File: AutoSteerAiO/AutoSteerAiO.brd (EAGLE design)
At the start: 114.3 x 99.1 mm, 88 parts, among them J4 CONNECTOR 1x5 PINS, K4 CB1A-P-12V, T1 BC547, U1 VX7805-1000

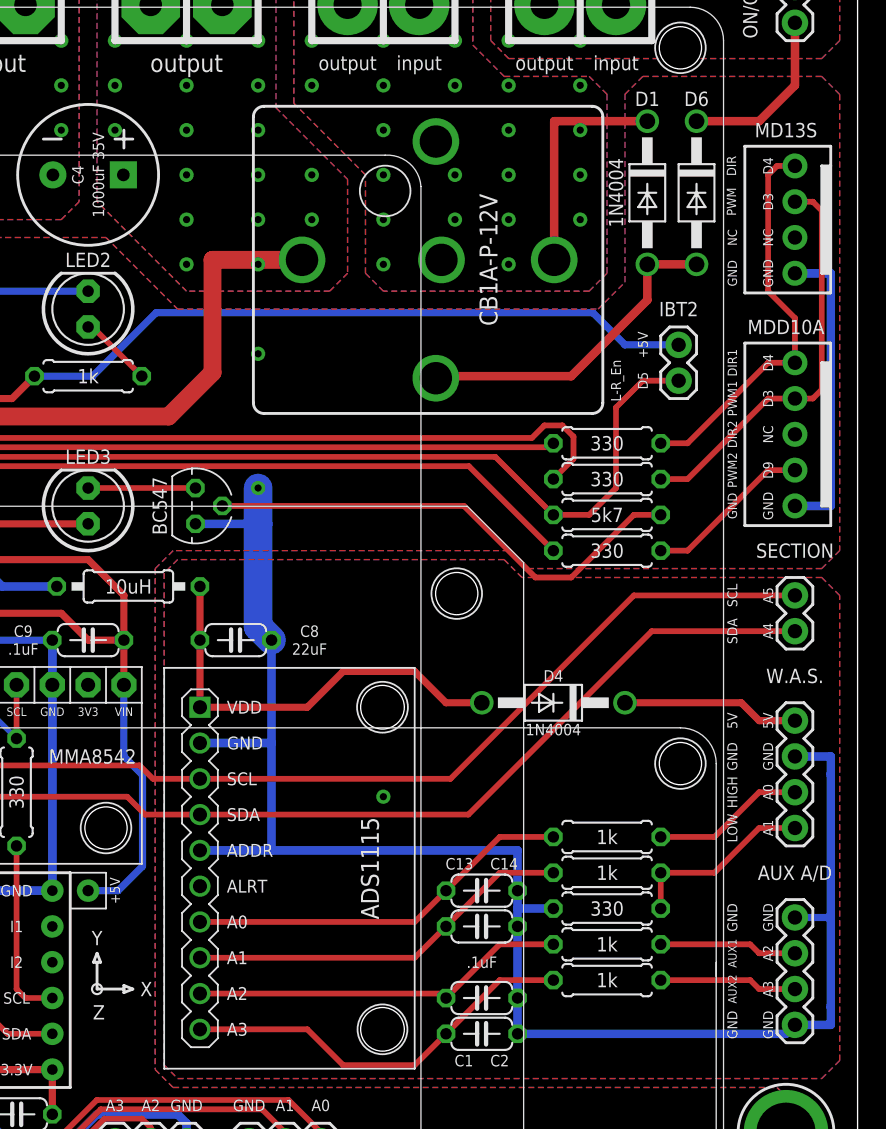
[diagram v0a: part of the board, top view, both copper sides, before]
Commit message: Add files via upload
One connector for all motor drivers
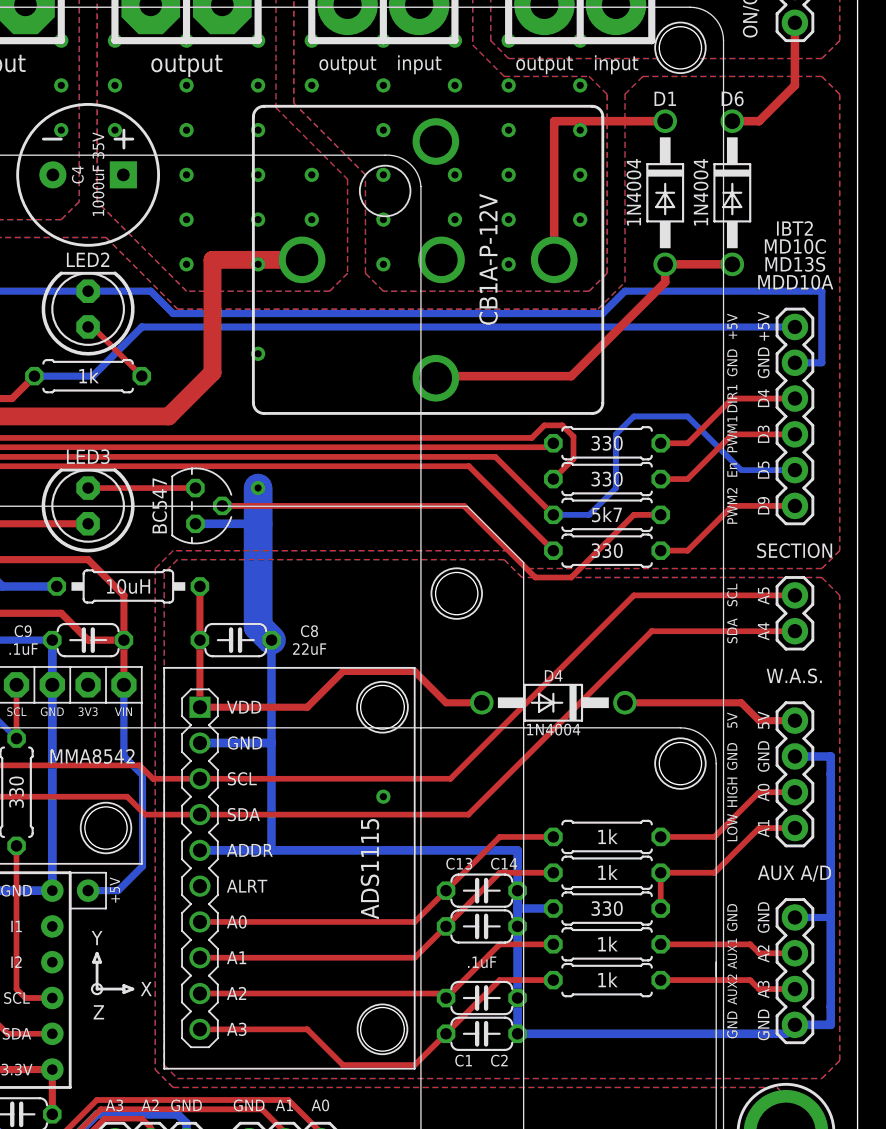
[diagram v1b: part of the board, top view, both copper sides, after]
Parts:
- removed D5: CONNECTOR 1x1 PIN, SparkFun-Connectors:1X02
- removed JP1: CONNECTOR 1x4 PINS, Header and Connector:2600-04
- J4: device Header and Connector:2600-05 -> SparkFun-Connectors:1X06
- moved D6 2.54 mm to (105.4, 71.8)
- moved D1 1.27 mm to (100.6, 71.8)
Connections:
- net +5V: now also J4.6; no longer D5.2
- net D5: now also J4.2; no longer D5.1
- net GND: now also J4.5; no longer J4.1, JP1.1
- net N$19: now also J4.4; no longer J4.5, JP1.4
- net N$20: now also J4.3; no longer J4.4, JP1.3
- net N$22: now also J4.1; no longer J4.2
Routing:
- net GND: track 526.2 -> 565.0 mm
- net N$20: track 28.9 -> 10.8 mm
- net N$19: track 28.2 -> 10.8 mm
- net D5: track 103.6 -> 111.2 mm
- net +5V: track 316.5 -> 323.4 mm
- net N$28: track 12.5 -> 9.94 mm
- net N$5: track 23.4 -> 25.2 mm
- net V+: track 16.4 -> 17.7 mm
- net N$22: track 11.9 -> 10.8 mm
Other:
- board text added: "D5"
- board text added: "En"
- board text removed: "DIR"
- board text removed: "DIR2"
- board text removed: "L-R_En"
- board text removed: "NC"
- board text removed: "PWM"

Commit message: Add files via upload
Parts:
- removed 15V1, 15V2, GND, GND30: WIREPAD4,16O1,6, wirepad:4,16O1,6
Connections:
- net +15V: no longer 15V1.1, 15V2.1
- net GND: no longer GND.1, GND30.1
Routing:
- net GND: vias 70 -> 72
- net +15V: vias 20 -> 22
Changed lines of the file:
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@@
 <setting verticaltext="up"/>
 </settings>
-<grid distance="50" unitdist="mil" unit="mil" style="lines" multiple="1" display="yes" altdistance="12.5" altunitdist="mil" altunit="mil"/>
+<grid distance="50" unitdist="mil" unit="mm" style="lines" multiple="1" display="yes" altdistance="12.5" altunitdist="mil" altunit="mil"/>
 <layers>
 <layer number="1" name="Top" color="4" fill="1" visible="yes" active="yes"/>
@@
 <attribute name="OC_NEWARK" value="unknown" x="109.855" y="86.36" size="1.778" layer="27" rot="R270" display="off"/>
 </element>
-<element name="15V1" library="wirepad" library_urn="urn:adsk.eagle:library:412" package="4,16O1,6" package3d_urn="urn:adsk.eagle:package:30843/1" value="WIREPAD4,16O1,6" x="69.215" y="85.09" smashed="yes" rot="R180">
-<attribute name="MF" value="" x="69.215" y="85.09" size="1.778" layer="27" rot="R180" display="off"/>
-<attribute name="MPN" value="" x="69.215" y="85.09" size="1.778" layer="27" rot="R180" display="off"/>
-<attribute name="OC_NEWARK" value="unknown" x="69.215" y="85.09" size="1.778" layer="27" rot="R180" display="off"/>
-</element>
-<element name="15V2" library="wirepad" library_urn="urn:adsk.eagle:library:412" package="4,16O1,6" package3d_urn="urn:adsk.eagle:package:30843/1" value="WIREPAD4,16O1,6" x="64.135" y="85.09" smashed="yes" rot="R180">
-<attribute name="MF" value="" x="64.135" y="85.09" size="1.778" layer="27" rot="R180" display="off"/>
-<attribute name="MPN" value="" x="64.135" y="85.09" size="1.778" layer="27" rot="R180" display="off"/>
-<attribute name="OC_NEWARK" value="unknown" x="64.135" y="85.09" size="1.778" layer="27" rot="R180" display="off"/>
-</element>
-<element name="GND" library="wirepad" library_urn="urn:adsk.eagle:library:412" package="4,16O1,6" package3d_urn="urn:adsk.eagle:package:30843/1" value="WIREPAD4,16O1,6" x="55.245" y="85.09" smashed="yes" rot="R180">
-<attribute name="MF" value="" x="55.245" y="85.09" size="1.778" layer="27" rot="R180" display="off"/>
-<attribute name="MPN" value="" x="55.245" y="85.09" size="1.778" layer="27" rot="R180" display="off"/>
-<attribute name="OC_NEWARK" value="unknown" x="55.245" y="85.09" size="1.778" layer="27" rot="R180" display="off"/>
-</element>
-<element name="GND30" library="wirepad" library_urn="urn:adsk.eagle:library:412" package="4,16O1,6" package3d_urn="urn:adsk.eagle:package:30843/1" value="WIREPAD4,16O1,6" x="50.165" y="85.09" smashed="yes" rot="R180">
-<attribute name="MF" value="" x="50.165" y="85.09" size="1.778" layer="27" rot="R180" display="off"/>
-<attribute name="MPN" value="" x="50.165" y="85.09" size="1.778" layer="27" rot="R180" display="off"/>
-<attribute name="OC_NEWARK" value="unknown" x="50.165" y="85.09" size="1.778" layer="27" rot="R180" display="off"/>
-</element>
 <element name="J4" library="SparkFun-Connectors" library_urn="urn:adsk.eagle:library:513" package="1X06" package3d_urn="urn:adsk.eagle:package:38009/1" value="CONNECTOR 1x5 PINS" x="109.855" y="49.53" smashed="yes" rot="R90">
 <attribute name="LABEL" value="" x="112.776" y="48.133" size="0.762" layer="21" font="vector" ratio="15" rot="R90" align="top-left"/>
@@
 <contactref element="C12" pad="1"/>
 <contactref element="C4" pad="-"/>
-<contactref element="GND30" pad="1"/>
-<contactref element="GND" pad="1"/>
 <contactref element="D3" pad="A"/>
 <contactref element="LED1" pad="K"/>
@@
 <via x="8.89" y="2.54" extent="1-16" drill="0.508"/>
 <via x="26.67" y="29.845" extent="1-16" drill="0.508"/>
-<via x="92.075" y="85.09" extent="1-16" drill="2" diameter="4.3" shape="square"/>
-<via x="97.155" y="85.09" extent="1-16" drill="2" diameter="4.3" shape="square"/>
+<via x="92.075" y="85.09" extent="1-16" drill="2.8" diameter="4.5" shape="square"/>
+<via x="97.155" y="85.09" extent="1-16" drill="2.8" diameter="4.5" shape="square"/>
 <contactref element="C5" pad="-"/>
 <via x="89.535" y="82.55" extent="1-16" drill="0.508"/>
@@
 <wire x1="111.76" y1="59.69" x2="111.76" y2="64.77" width="0.508" layer="16"/>
 <wire x1="111.76" y1="64.77" x2="97.79" y2="64.77" width="0.508" layer="16"/>
+<via x="55.245" y="85.09" extent="1-16" drill="2.8" diameter="4.5" shape="square"/>
+<via x="50.165" y="85.09" extent="1-16" drill="2.8" diameter="4.5" shape="square"/>
 </signal>
 <signal name="D5">
@@
 </signal>
 <signal name="V+">
-<via x="83.185" y="85.09" extent="1-16" drill="2" diameter="4.3" shape="square"/>
-<via x="78.105" y="85.09" extent="1-16" drill="2" diameter="4.3" shape="square" alwaysstop="yes"/>
+<via x="83.185" y="85.09" extent="1-16" drill="2.8" diameter="4.5" shape="square"/>
+<via x="78.105" y="85.09" extent="1-16" drill="2.8" diameter="4.5" shape="square" alwaysstop="yes"/>
 <contactref element="K4" pad="87"/>
 <contactref element="K4" pad="85"/>
@@
 <signal name="+15V">
 <contactref element="C4" pad="+"/>
-<contactref element="15V1" pad="1"/>
-<contactref element="15V2" pad="1"/>
 <contactref element="R12" pad="1"/>
 <contactref element="R13" pad="1"/>
@@
 <wire x1="10.16" y1="18.415" x2="6.35" y2="18.415" width="0.6096" layer="1"/>
 <wire x1="6.35" y1="18.415" x2="5.08" y2="17.145" width="0.6096" layer="1"/>
+<via x="69.215" y="85.09" extent="1-16" drill="2.8" diameter="4.5" shape="square"/>
+<via x="64.135" y="85.09" extent="1-16" drill="2.8" diameter="4.5" shape="square"/>
 </signal>
 <signal name="HIGH">

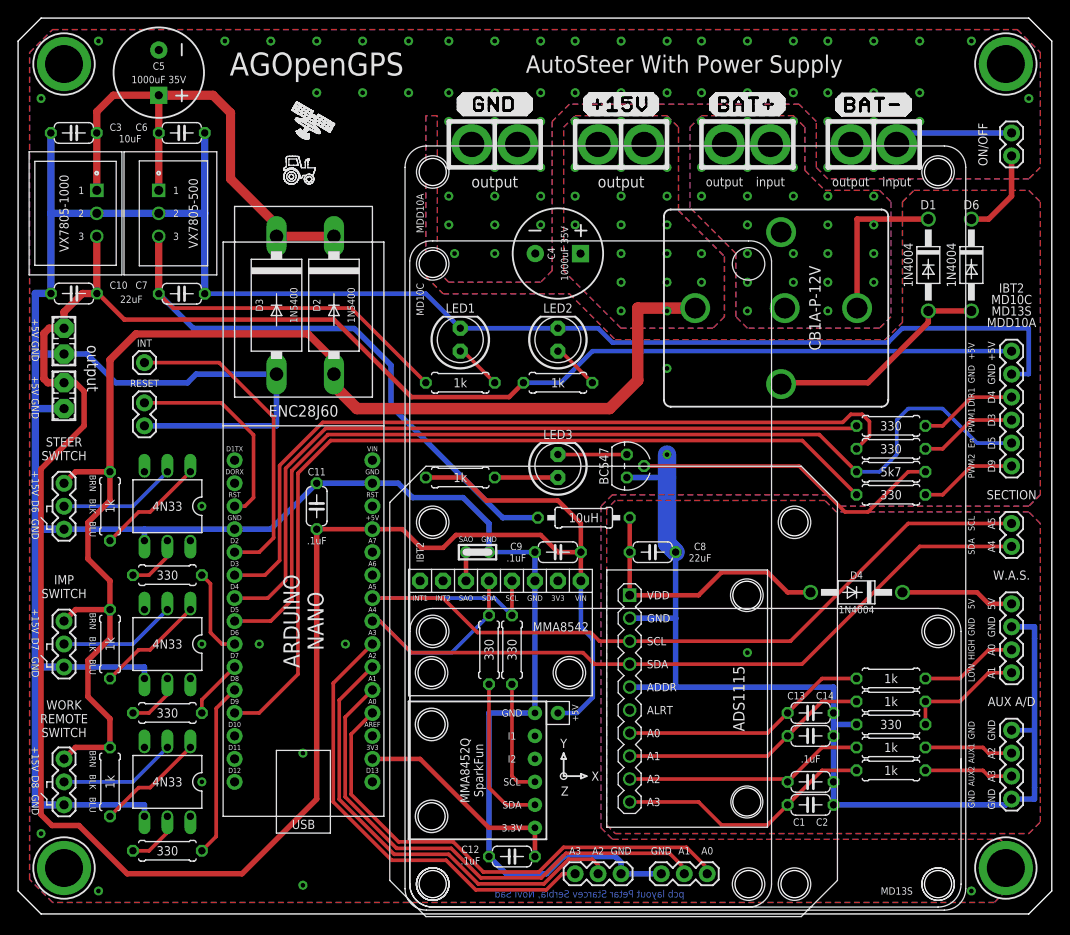
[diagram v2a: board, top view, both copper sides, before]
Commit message: Add files via upload
Added connector for SWEncoder
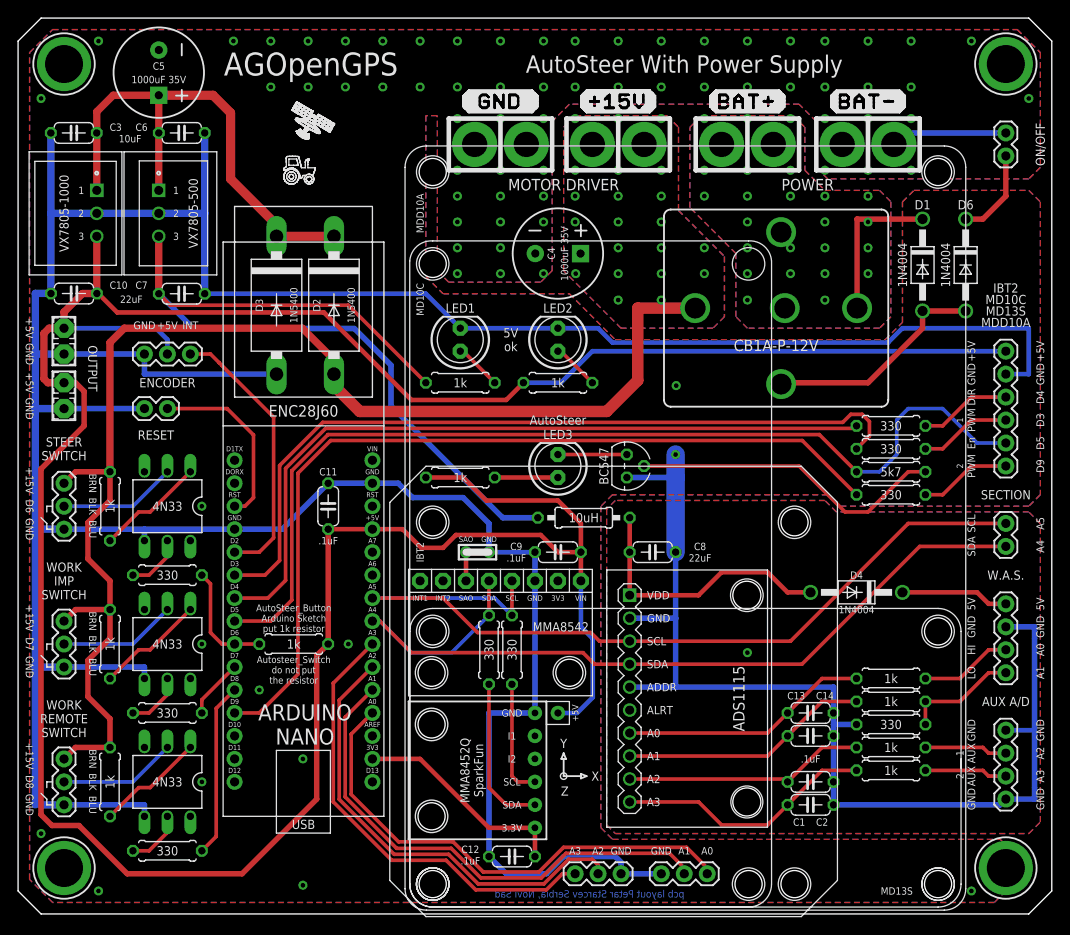
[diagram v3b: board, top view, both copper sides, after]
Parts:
- added R15: 1k, resistor:0207/7
- INT: value CONNECTOR 1x1 PIN -> (none); device SparkFun-Connectors:1X01 -> SparkFun-Connectors:1X03
- moved INT 5.17 mm to (19.1, 61.9), turned to 180 degrees
- moved RESET 1.91 mm to (14.0, 55.9), turned to 0 degrees
- moved U$11 1.91 mm to (78.1, 54.0)
- moved C11 1.27 mm to (34.3, 45.1)
- moved U$12 1.27 mm to (80.6, 48.9)
- moved AUX_A/D 0.64 mm to (109.2, 12.7)
- moved J4 0.64 mm to (109.2, 49.5)
- moved ON/OFF 0.64 mm to (109.2, 86.4)
- moved TO_SECTION 0.64 mm to (109.2, 43.2)
- moved WAS_D 0.64 mm to (109.2, 34.3)
- moved D1 0.63 mm to (100.0, 71.8)
- moved D6 0.63 mm to (104.8, 71.8)
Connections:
- net +5V: now also INT.2, R15.1
- net D6: now also R15.2
- net GND: now also INT.3
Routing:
- net +5V: track 323.4 -> 335.8 mm
- net GND: track 565.0 -> 556.2 mm, vias 72 -> 80
- net D2: track 35.1 -> 30.4 mm
- net RST: track 22.9 -> 20.1 mm
- net D6: track 9.94 -> 12.7 mm
- net +15V: track 144.0 -> 145.9 mm, vias 22 -> 23
- net SCL: track 98.1 -> 97.4 mm
- net SDA: track 97.9 -> 97.3 mm
- net N$22: track 10.8 -> 10.2 mm
- net N$21: track 12.6 -> 12.0 mm
- net N$20: track 10.8 -> 10.2 mm
- net N$19: track 10.8 -> 10.2 mm
- net N$11: track 9.79 -> 9.15 mm
- net N$10: track 9.79 -> 9.15 mm
- net LOW.: track 13.4 -> 12.7 mm
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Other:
- board text added: "1"
- board text added: "1k"
- board text added: "2"
- board text added: "5V ok"
- board text added: "AUX"
- board text added: "AutoSteer"
- board text added: "AutoSteer_Button Arduino Sketch put 1k resistor Autosteer_Switch do not put the resistor"
- board text added: "DIR"
- board text added: "ENCODER"
- board text added: "HI"
- board text added: "LO"
- board text added: "MOTOR DRIVER"
- board text added: "OUTPUT"
- board text added: "POWER"
- board text added: "PWM"
- board text added: "WORK IMP SWITCH"
- board text removed: "AUX1"
- board text removed: "AUX2"
- board text removed: "DIR1"
- board text removed: "HIGH"
- board text removed: "IMP SWITCH"
- board text removed: "LOW"
- board text removed: "PWM1"
- board text removed: "PWM2"
- board text removed: "input"
- board text removed: "output"
